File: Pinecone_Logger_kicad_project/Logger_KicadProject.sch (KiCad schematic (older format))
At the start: 42 parts, among them J1 PJ-102A, J2 M50-3600542, J3 DM3AT-SF-PEJM5, J4 OSTVN06A150, J5 OSTVN06A150, J6 OSTVN06A150, J7 OSTVN06A150, J8 10_Pin_Header, Q1 AO3420, Q2 AO3420, U1 SAMD20E16A-A, U2 MIC5211, U3 AP2281, U4 DS3231, U5 MAX4618, U6 MAX31856

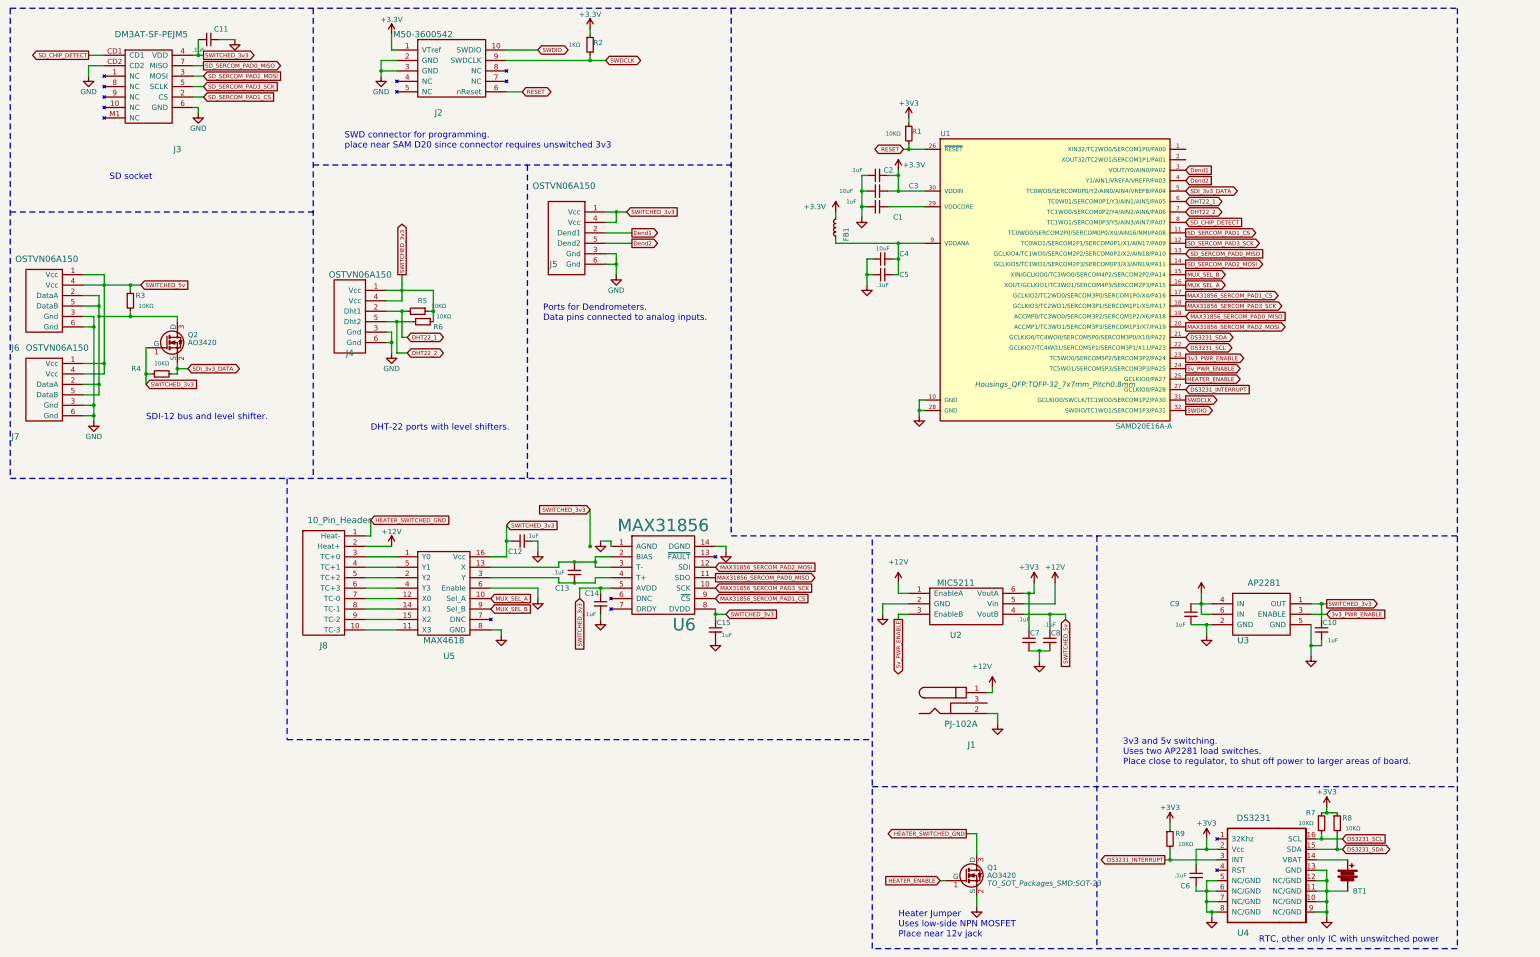
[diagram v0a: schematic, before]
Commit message: Finished Logger V2 design, ready for pcb order
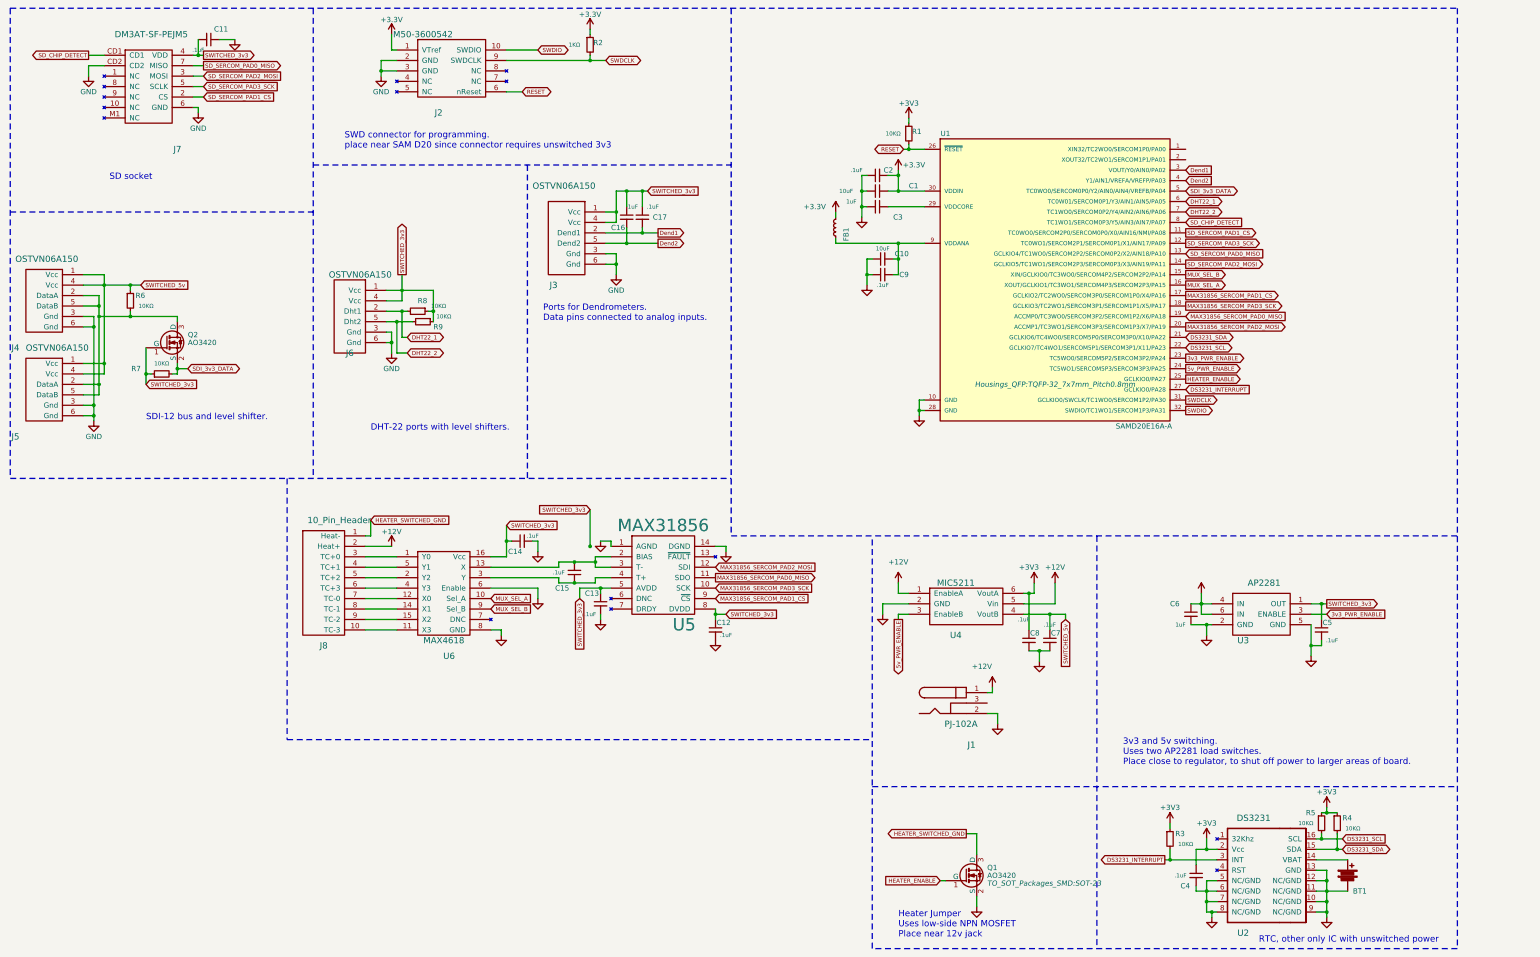
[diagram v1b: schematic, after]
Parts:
- added C16, C17: C0805C104K5RACTU, Capacitors_SMD:C_0805, symbol C_Small
- renumbered C3 to C1, C4 to C10, C15 to C12, C14 to C13, C12 to C14, C13 to C15, C1 to C3, C6 to C4, C10 to C5, C9 to C6, C8 to C7, C7 to C8, C5 to C9, J5 to J3, J6 to J4, J7 to J5, J4 to J6, J3 to J7, R9 to R3, R8 to R4, R7 to R5, R3 to R6, R4 to R7, R5 to R8, R6 to R9, U4 to U2, U2 to U4, U6 to U5, U5 to U6
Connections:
- net Dend1: now also C17.2
- net Dend2: now also C16.2
- net SWITCHED_3v3: now also C16.1, C17.1

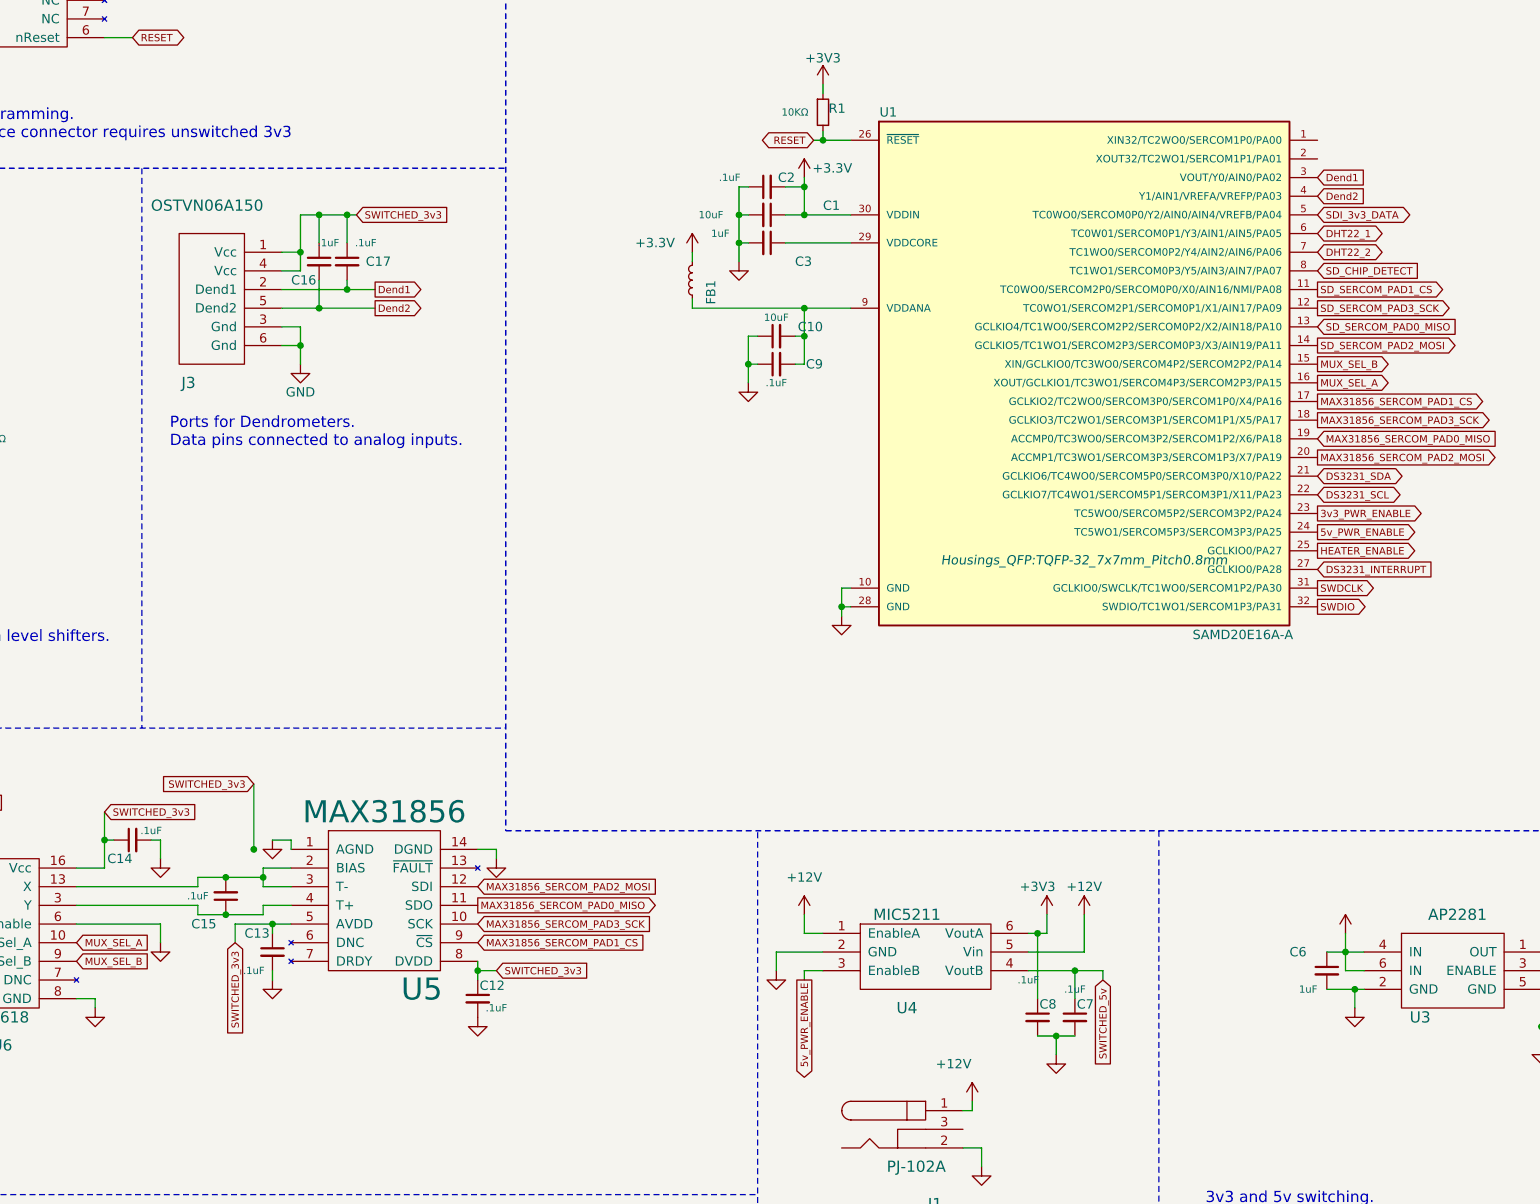
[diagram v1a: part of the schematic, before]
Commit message: logger circuit design finished, and ordered
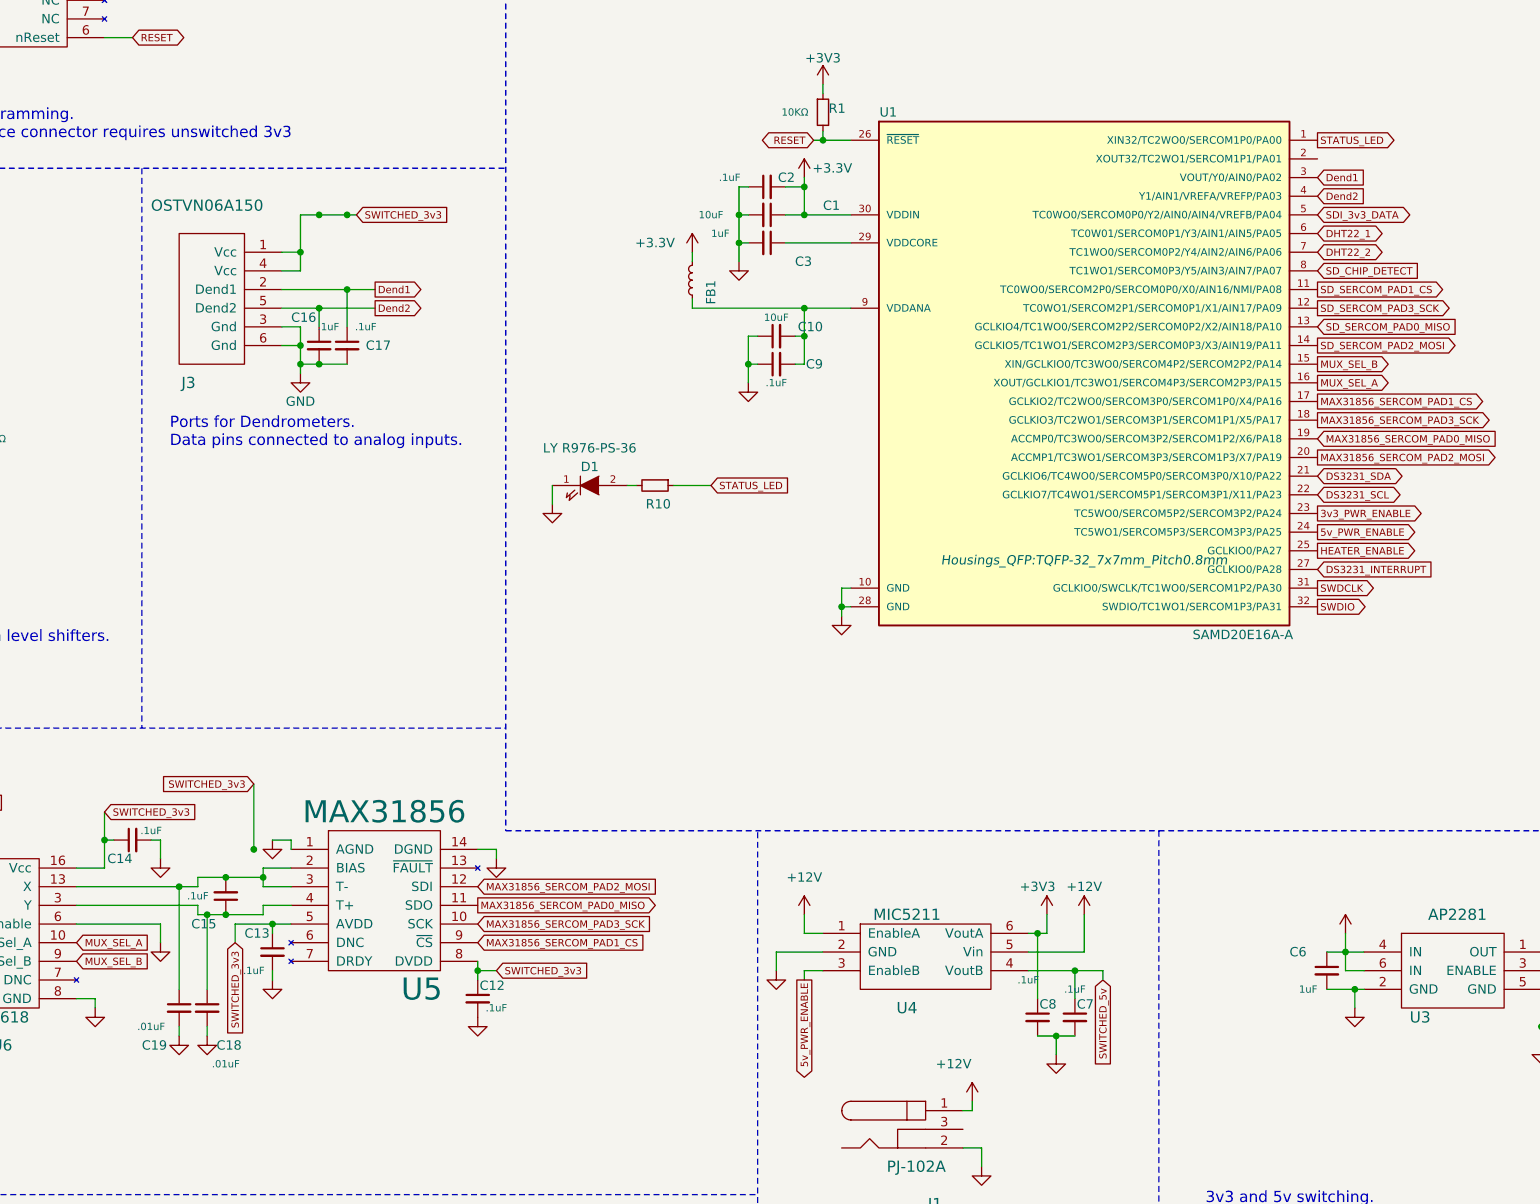
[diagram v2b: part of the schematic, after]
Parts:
- added C18, C19: C0805C103K5RACTU, Capacitors_SMD:C_0805, symbol C_Small
- added D1: LY R976-PS-36, LEDs:LED_0805, symbol LED
- added R10: RC0805JR-0768RL, Resistors_SMD:R_0805, symbol R_Small
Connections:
- net Dend1: now also C17.1; no longer C17.2
- net Dend2: now also C16.1; no longer C16.2
- net GND: now also C16.2, C17.2, C18.2, C19.2, D1.1 (K)
- net SWITCHED_3v3: no longer C16.1, C17.1
- net at C15.1, U5.4 (T+), U6.3 (Y): now also C18.1
- net at C15.2, U5.2 (BIAS), U5.3 (T-)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: now also C19.1
- net STATUS_LED: now reaches U1.1 (XIN32/TC2WO0/SERCOM1P0/PA00)
- net STATUS_LED: now also R10.1
- new net: D1.2 (A), R10.2
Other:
- moved on the sheet: C16, C17
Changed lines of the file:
@@
 L GND #PWR02
 U 1 1 58533060
-P 7900 3050
-F 0 "#PWR02" H 7900 2800 50  0001 C CNN
-F 1 "GND" H 7900 2900 50  0000 C CNN
-F 2 "" H 7900 3050 50  0000 C CNN
-F 3 "" H 7900 3050 50  0000 C CNN
-	1    7900 3050
+P 7900 3100
+F 0 "#PWR02" H 7900 2850 50  0001 C CNN
+F 1 "GND" H 7900 2950 50  0000 C CNN
+F 2 "" H 7900 3100 50  0000 C CNN
+F 3 "" H 7900 3100 50  0000 C CNN
+	1    7900 3100
 	1    0    0    -1
 $EndComp
@@
 	7800 2950 7900 2950
 Wire Wire Line
-	7900 2850 7900 3050
+	7900 2850 7900 3100
 Wire Wire Line
 	7800 2850 7900 2850
@@
 L C_Small C16
 U 1 1 58B9D99C
-P 8000 2500
-F 0 "C16" H 7850 2400 50  0000 L CNN
-F 1 "C0805C104K5RACTU" V 8000 2650 50  0001 L CNN
-F 2 "Capacitors_SMD:C_0805" H 8000 2500 50  0001 C CNN
-F 3 "" H 8000 2500 50  0000 C CNN
-F 4 ".1uF" H 8050 2600 39  0000 C CNN "Capacitance"
-	1    8000 2500
+P 8000 2950
+F 0 "C16" H 7850 3100 50  0000 L CNN
+F 1 "C0805C104K5RACTU" V 8000 3100 50  0001 L CNN
+F 2 "Capacitors_SMD:C_0805" H 8000 2950 50  0001 C CNN
+F 3 "" H 8000 2950 50  0000 C CNN
+F 4 ".1uF" H 8050 3050 39  0000 C CNN "Capacitance"
+	1    8000 2950
 	1    0    0    -1
 $EndComp
@@
 L C_Small C17
 U 1 1 58B9DF9A
-P 8150 2500
-F 0 "C17" H 8250 2500 50  0000 L CNN
-F 1 "C0805C104K5RACTU" V 8150 2650 50  0001 L CNN
-F 2 "Capacitors_SMD:C_0805" H 8150 2500 50  0001 C CNN
-F 3 "" H 8150 2500 50  0000 C CNN
-F 4 ".1uF" H 8250 2600 39  0000 C CNN "Capacitance"
-	1    8150 2500
-	1    0    0    -1
-$EndComp
-Wire Wire Line
-	8000 2750 8000 2600
+P 8150 2950
+F 0 "C17" H 8250 2950 50  0000 L CNN
+F 1 "C0805C104K5RACTU" V 8150 3100 50  0001 L CNN
+F 2 "Capacitors_SMD:C_0805" H 8150 2950 50  0001 C CNN
+F 3 "" H 8150 2950 50  0000 C CNN
+F 4 ".1uF" H 8250 3050 39  0000 C CNN "Capacitance"
+	1    8150 2950
+	1    0    0    -1
+$EndComp
 Connection ~ 8000 2750
-Wire Wire Line
-	8150 2650 8150 2600
 Connection ~ 8150 2650
 Wire Wire Line
-	8150 2400 8150 2250
-Wire Wire Line
 	7900 2250 8200 2250
-Wire Wire Line
-	8000 2400 8000 2250
 Connection ~ 8150 2250
 Connection ~ 8000 2250
+$Comp
+L C_Small C18
+U 1 1 58BA3AE6
+P 7400 6500
+F 0 "C18" H 7450 6300 50  0000 L CNN
+F 1 "C0805C103K5RACTU" H 7410 6420 50  0001 L CNN
+F 2 "Capacitors_SMD:C_0805" H 7400 6500 50  0001 C CNN
+F 3 "" H 7400 6500 50  0000 C CNN
+F 4 ".01uF" H 7500 6200 39  0000 C CNN "Capacitance"
+	1    7400 6500
+	1    0    0    -1
+$EndComp
+$Comp
+L C_Small C19
+U 1 1 58BA3C69
+P 7250 6500
+F 0 "C19" H 7050 6300 50  0000 L CNN
+F 1 "C0805C103K5RACTU" H 7260 6420 50  0001 L CNN
+F 2 "Capacitors_SMD:C_0805" H 7250 6500 50  0001 C CNN
+F 3 "" H 7250 6500 50  0000 C CNN
+F 4 ".01uF" H 7100 6400 39  0000 C CNN "Capacitance"
+	1    7250 6500
+	1    0    0    -1
+$EndComp
+Wire Wire Line
+	7400 6000 7400 6400
+Connection ~ 7400 6000
+Wire Wire Line
+	7250 6400 7250 5850
+Connection ~ 7250 5850
+$Comp
+L GND #PWR040
+U 1 1 58BA4624
+P 7400 6650
+F 0 "#PWR040" H 7400 6400 50  0001 C CNN
+F 1 "GND" H 7400 6500 50  0001 C CNN
+F 2 "" H 7400 6650 50  0000 C CNN
+F 3 "" H 7400 6650 50  0000 C CNN
+	1    7400 6650
+	1    0    0    -1
+$EndComp
+$Comp
+L GND #PWR041
+U 1 1 58BA46B9
+P 7250 6650
+F 0 "#PWR041" H 7250 6400 50  0001 C CNN
+F 1 "GND" H 7250 6500 50  0001 C CNN
+F 2 "" H 7250 6650 50  0000 C CNN
+F 3 "" H 7250 6650 50  0000 C CNN
+	1    7250 6650
+	1    0    0    -1
+$EndComp
+Wire Wire Line
+	7250 6600 7250 6650
+Wire Wire Line
+	7400 6600 7400 6650
+Text GLabel 13350 1850 2    39   Output ~ 0
+STATUS_LED
+Text GLabel 10100 3700 2    39   Input ~ 0
+STATUS_LED
+$Comp
+L LED D1
+U 1 1 58BDB7E6
+P 9450 3700
+F 0 "D1" H 9450 3800 50  0000 C CNN
+F 1 "LY R976-PS-36" H 9450 3900 50  0000 C CNN
+F 2 "LEDs:LED_0805" H 9450 3700 50  0001 C CNN
+F 3 "" H 9450 3700 50  0000 C CNN
+	1    9450 3700
+	1    0    0    -1
+$EndComp
+Wire Wire Line
+	9900 3700 10100 3700
+$Comp
+L R_Small R10
+U 1 1 58BDBC1A
+P 9800 3700
+F 0 "R10" V 9900 3650 50  0000 L CNN
+F 1 "RC0805JR-0768RL" H 9830 3660 50  0001 L CNN
+F 2 "Resistors_SMD:R_0805" H 9800 3700 50  0001 C CNN
+F 3 "" H 9800 3700 50  0000 C CNN
+F 4 "68 Ohm" H 9800 3700 60  0001 C CNN "Resistance"
+	1    9800 3700
+	0    1    1    0
+$EndComp
+$Comp
+L GND #PWR042
+U 1 1 58BDBEB8
+P 9250 3800
+F 0 "#PWR042" H 9250 3550 50  0001 C CNN
+F 1 "GND" H 9250 3650 50  0001 C CNN
+F 2 "" H 9250 3800 50  0000 C CNN
+F 3 "" H 9250 3800 50  0000 C CNN
+	1    9250 3800
+	1    0    0    -1
+$EndComp
+Wire Wire Line
+	9250 3700 9250 3800
+Wire Wire Line
+	9700 3700 9650 3700
+Wire Wire Line
+	8000 2750 8000 2850
+Wire Wire Line
+	8150 2650 8150 2850
+Wire Wire Line
+	7900 3050 8150 3050
+Connection ~ 8000 3050
+Connection ~ 7900 3050
 $EndSCHEMATC

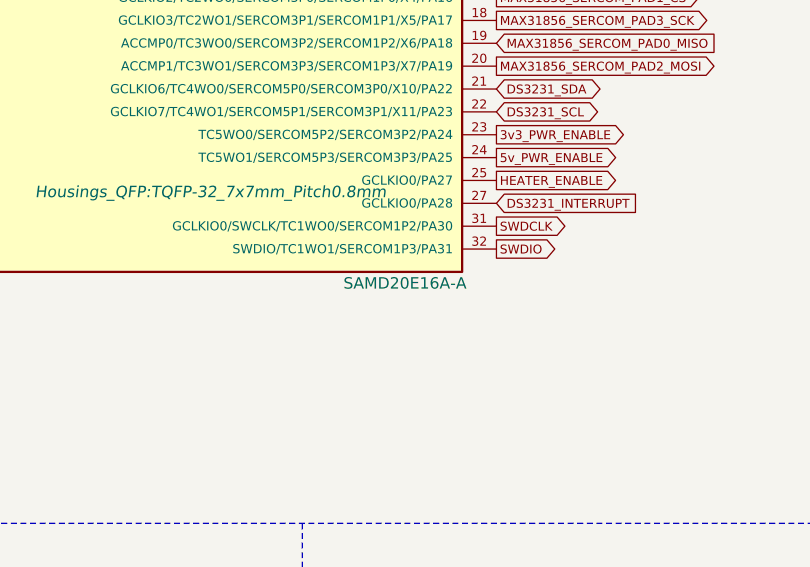
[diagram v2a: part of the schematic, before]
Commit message: updated schematic and pcb to correctly use SAM D20 E18, not the E16
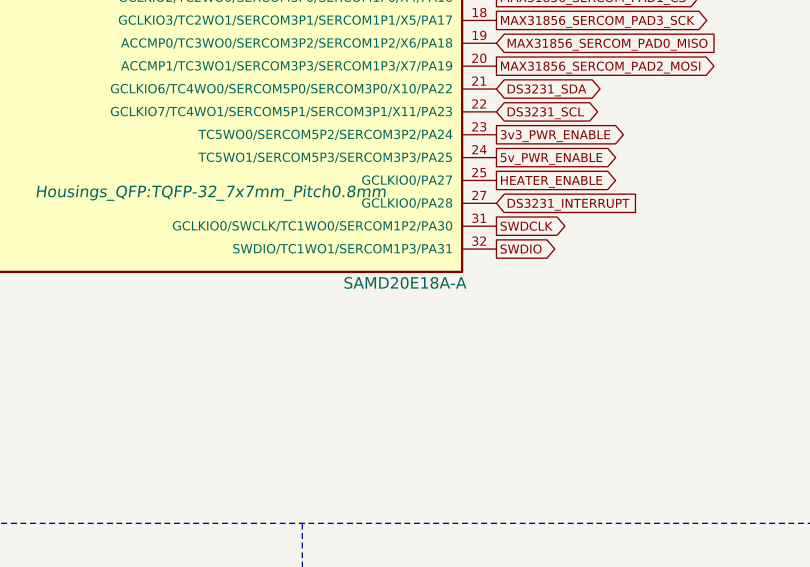
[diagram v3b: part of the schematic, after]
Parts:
- U1: value SAMD20E16A-A -> SAMD20E18A-A
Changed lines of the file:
@@
 P 12100 3100
 F 0 "U1" H 11050 4500 50  0000 C CNN
-F 1 "SAMD20E16A-A" H 12950 1700 50  0000 C CNN
+F 1 "SAMD20E18A-A" H 12950 1700 50  0000 C CNN
 F 2 "Housings_QFP:TQFP-32_7x7mm_Pitch0.8mm" H 12100 2100 50  0000 C CIN
 F 3 "" H 12100 3100 50  0000 C CNN

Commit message: finally fixed MAX31856, oh god
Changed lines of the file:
@@
 Text GLabel 6850 5450 2    39   Input ~ 0
-SWITCHED_3v3
-Text GLabel 7650 5300 0    39   Input ~ 0
 SWITCHED_3v3
 Text GLabel 3350 3150 2    39   Input ~ 0
@@
 Wire Wire Line
 	7750 6350 7750 6300
-Connection ~ 7650 5650
-Wire Wire Line
-	7650 5300 7650 5650
 Wire Wire Line
 	5550 5550 5550 5400
